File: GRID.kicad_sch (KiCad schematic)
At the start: 9 parts, among them J501 Conn_01x04, J502 Conn_01x04, J503 Conn_01x04, J504 Conn_01x04, J505 Conn_01x04, J506 Conn_01x04, J507 Conn_01x04, J508 Conn_01x04, M501 Conn_01x08

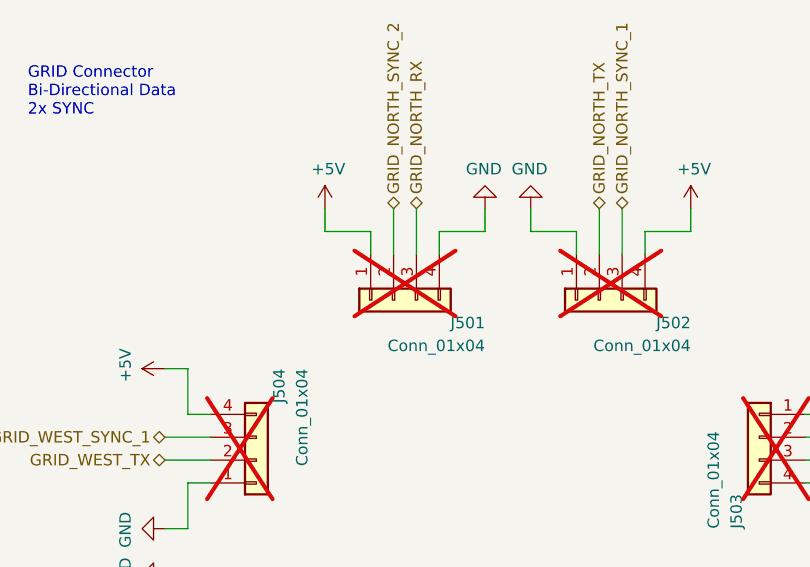
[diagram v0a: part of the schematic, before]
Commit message: Adds traces
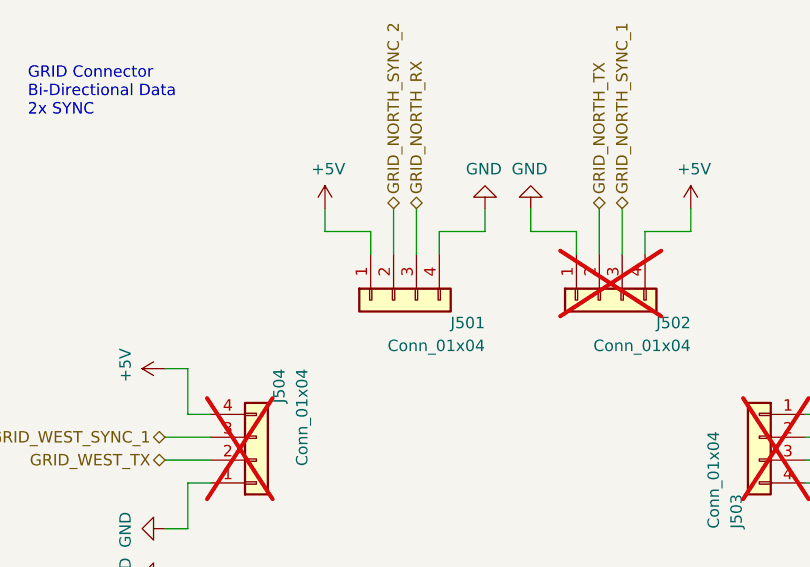
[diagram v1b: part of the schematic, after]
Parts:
- J501: footprint suku_basics:J_INTERFACE_SPRINGPATTERN -> Connector_Molex:Molex_Nano-Fit_105309-xx04_1x04_P2.50mm_Vertical; now fitted
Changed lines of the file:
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@@
 		(exclude_from_sim no)
 		(in_bom no)
-		(on_board no)
-		(dnp yes)
+		(on_board yes)
+		(dnp no)
 		(property "Reference" "J501"
 			(at 73.66 50.8 90)
@@
 			)
 		)
-		(property "Footprint" "suku_basics:J_INTERFACE_SPRINGPATTERN"
+		(property "Footprint" "Connector_Molex:Molex_Nano-Fit_105309-xx04_1x04_P2.50mm_Vertical"
 			(at 63.5 48.26 0)
 			(effects

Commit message: Updates F.Silkscreen
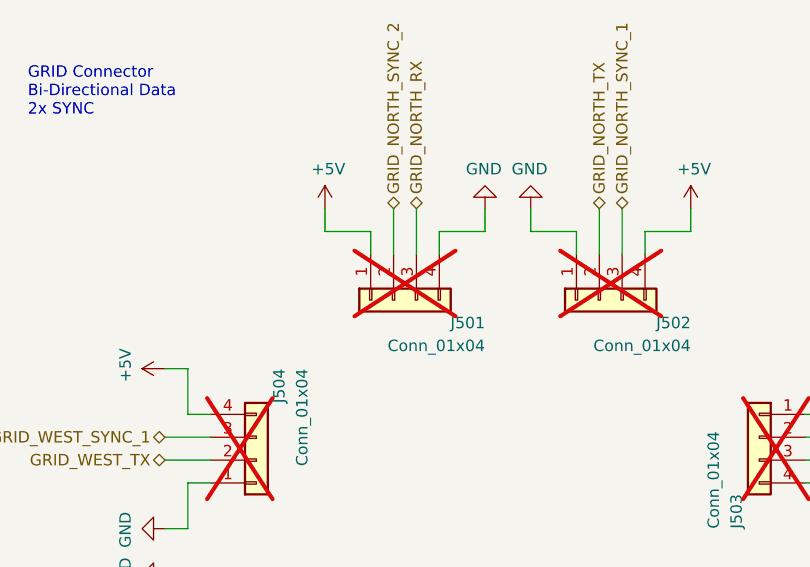
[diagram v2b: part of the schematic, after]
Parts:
- J501: now not fitted
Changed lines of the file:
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@@
 		(exclude_from_sim no)
 		(in_bom no)
-		(on_board yes)
-		(dnp no)
+		(on_board no)
+		(dnp yes)
 		(property "Reference" "J501"
 			(at 73.66 50.8 90)
